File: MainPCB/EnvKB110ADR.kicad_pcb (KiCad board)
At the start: 2 copper layers, 429.5 x 123.7 mm, 231 parts, among them U1 XC6206PxxxMR, U2 STM32F411CEUx

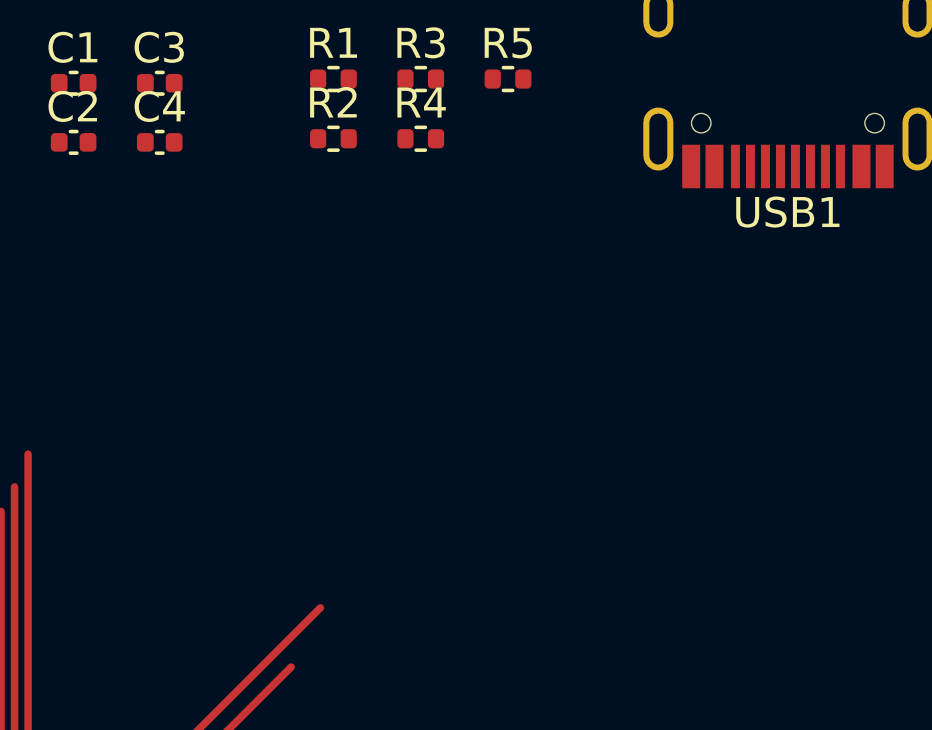
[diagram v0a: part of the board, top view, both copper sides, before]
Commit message: Updated PCB to have new parts
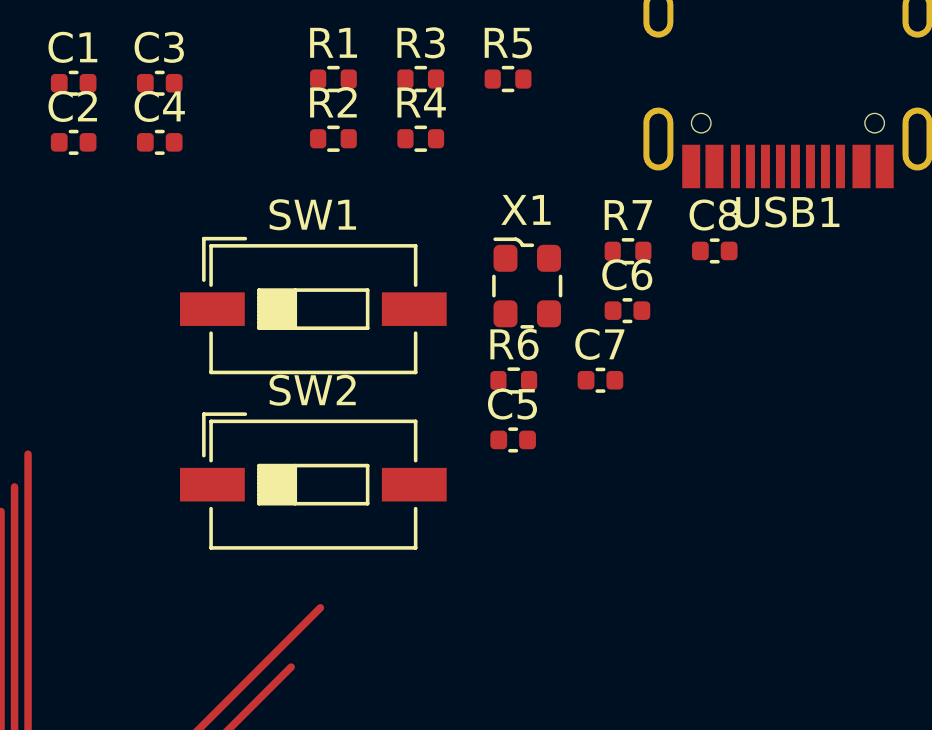
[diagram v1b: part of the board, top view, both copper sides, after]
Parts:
- added C5: 1uf capacitor, Capacitor_SMD:C_0402_1005Metric, F.Cu at (426.3, 69.7)
- added C6: 1uf capacitor, Capacitor_SMD:C_0402_1005Metric, F.Cu at (430.1, 65.4)
- added C7: 100nf 0402, Capacitor_SMD:C_0402_1005Metric, F.Cu at (429.2, 67.7)
- added C8: 100nf 0402, Capacitor_SMD:C_0402_1005Metric, F.Cu at (433.0, 63.4)
- added R6: 100k 0402, Resistor_SMD:R_0402_1005Metric, F.Cu at (426.3, 67.7)
- added R7: 10K 0402, Resistor_SMD:R_0402_1005Metric, F.Cu at (430.1, 63.4)
- added SW1: Boot Mode, Button_Switch_SMD:SW_DIP_SPSTx01_Slide_6.7x4.1mm_W6.73mm_P2.54mm_LowProfile_JPin, F.Cu at (419.6, 65.3)
- added SW2: Reset Switch, Button_Switch_SMD:SW_DIP_SPSTx01_Slide_6.7x4.1mm_W6.73mm_P2.54mm_LowProfile_JPin, F.Cu at (419.6, 71.2)
- added X1: ECS-2520MV-xxx-xx, Oscillator:Oscillator_SMD_ECS_2520MV-xxx-xx-4Pin_2.5x2.0mm, F.Cu at (426.8, 64.5)
- R1: value 1.5K -> 1.5K 0402
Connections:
- C1 pad 1: GND -> +3V3
- C1 pad 2: +3V3 -> GND
- U2 pad 44: (no net) -> boot0
- U2 pad 5: (no net) -> OSCpin
- U2 pad 7: (no net) -> resetsw

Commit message: Added row/col pins in the schematic for pcbnew to show them
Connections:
- U2 pad 10: (no net) -> col15
- U2 pad 11: (no net) -> col16
- U2 pad 12: (no net) -> col17
- U2 pad 14: (no net) -> col19
- U2 pad 15: (no net) -> col20
- U2 pad 16: (no net) -> col21
- U2 pad 17: (no net) -> col22
- U2 pad 18: (no net) -> col0
- U2 pad 19: (no net) -> col1
- U2 pad 20: (no net) -> col2
- U2 pad 21: (no net) -> col10
- U2 pad 23: GND -> (no net)
- U2 pad 25: (no net) -> col11
- U2 pad 26: (no net) -> col12
- U2 pad 27: (no net) -> col13
- U2 pad 28: (no net) -> col14
- U2 pad 29: (no net) -> row6
- U2 pad 30: (no net) -> row1
- U2 pad 31: (no net) -> row7
- U2 pad 34: (no net) -> row3
- U2 pad 35: GND -> (no net)
- U2 pad 37: (no net) -> row4
- U2 pad 38: (no net) -> row5
- U2 pad 39: (no net) -> col3
- U2 pad 40: (no net) -> col4
- U2 pad 41: (no net) -> col5
- U2 pad 42: (no net) -> col6
- U2 pad 43: (no net) -> col7
- U2 pad 45: (no net) -> col8
- U2 pad 46: (no net) -> col9
- U2 pad 47: GND -> (no net)

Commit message: See List
- Added ANSI support
- redone sections of the board to fit ansi support
- edited all footprints to have through holes so they can be connected on both sides.
- probably a bunch of other shite
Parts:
- added D_ANSI_1: SOD-123, Diode_SMD:D_SOD-123, B.Cu at (318.5, 114.1)
- added K_ANSI_1: KEYSW, MX_Only:MXOnly-2.25U-Hotswap, F.Cu at (59.0, 146.8)
- added K_ANSI_2: KEYSW, MX_Only:MXOnly-2.25U-Hotswap, F.Cu at (301.9, 127.7)
- added K_ANSI_3: KEYSW, MX_Only:MXOnly-1.5U-Hotswap, F.Cu at (309.1, 108.7)
- moved D_62 27.0 mm to (299.7, 135.8)
- moved D_82 11.1 mm to (296.1, 118.0), turned to 180 degrees
- moved D_86 7.37 mm to (58.4, 155.4), turned to 180 degrees
- turned K_62 to 90 degrees
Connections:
- D_62 pad 1: row4 -> row5
- H1 pad 1: (no net) -> GND
- H10 pad 1: (no net) -> GND
- H2 pad 1: (no net) -> GND
- H3 pad 1: (no net) -> GND
- H4 pad 1: (no net) -> GND
- H5 pad 1: (no net) -> GND
- H6 pad 1: (no net) -> GND
- H8 pad 1: (no net) -> GND
- H9 pad 1: (no net) -> GND
- U2 pad 1: (no net) -> Net-(U2-Pad1)
- U2 pad 13: (no net) -> col18
- U2 pad 2: (no net) -> Net-(U2-Pad2)
- U2 pad 22: (no net) -> Net-(U2-Pad22)
- U2 pad 23: (no net) -> Net-(U2-Pad23)
- U2 pad 3: (no net) -> Net-(U2-Pad3)
- U2 pad 35: (no net) -> Net-(U2-Pad35)
- U2 pad 4: (no net) -> Net-(U2-Pad4)
- U2 pad 47: (no net) -> Net-(U2-Pad47)
- U2 pad 6: (no net) -> Net-(U2-Pad6)
- USB1 pad 3: (no net) -> Net-(USB1-Pad3)
- USB1 pad 9: (no net) -> Net-(USB1-Pad9)
- X1 pad 1: (no net) -> Net-(X1-Pad1)
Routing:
- net col0: track 145.5 -> 173.5 mm, vias 6 -> 0
- net col14: track 133.8 -> 106.4 mm, vias 3 -> 0
- net Net-(D_62-Pad2): track 11.5 -> 29.6 mm, vias 0 -> 1
- net row5: track 438.4 -> 455.3 mm
- net col1: track 123.4 -> 138.8 mm, vias 3 -> 0
- net Net-(D_ANSI_1-Pad2): track 0.00 -> 11.3 mm
- net Net-(D_86-Pad2): track 7.11 -> 17.7 mm
- net col13: track 116.6 -> 108.0 mm, vias 4 -> 0
- net col12: track 71.3 -> 63.2 mm, vias 3 -> 0
- net col11: track 113.8 -> 106.1 mm, vias 5 -> 0
- net col15: track 112.1 -> 104.8 mm, vias 4 -> 0
- net col10: track 113.5 -> 106.3 mm, vias 5 -> 0
- net row6: track 473.9 -> 476.6 mm
- net row4: track 434.8 -> 437.1 mm, vias 1 -> 2
- net row1: vias 1 -> 0
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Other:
- board size 429.5 x 123.7 mm -> 429.5 x 125 mm

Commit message: more progress, working on column traces.
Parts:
- SW1, SW2: footprint Button_Switch_SMD:SW_DIP_SPSTx01_Slide_6.7x4.1mm_W6.73mm_P2.54mm_LowProfile_JPin -> Button_Switch_SMD:SW_Push_SPST_NO_Alps_SKRK
- moved D_12 9.52 mm to (55.6, 63.1)
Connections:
- U2 pad 23: Net-(U2-Pad23) -> GND
- U2 pad 35: Net-(U2-Pad35) -> GND
- U2 pad 47: Net-(U2-Pad47) -> GND
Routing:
- net col2: track 86.2 -> 422.8 mm
- net col0: track 173.5 -> 503.4 mm
- net col3: track 111.2 -> 428.7 mm
- net col1: track 138.8 -> 441.0 mm
- net col4: track 86.1 -> 384.3 mm
- net col5: track 86.1 -> 365.1 mm
- net col7: track 85.9 -> 330.6 mm
- net col6: track 106.1 -> 337.3 mm
- net col8: track 86.3 -> 311.3 mm
- net col9: track 86.3 -> 292.1 mm
- net col10: track 106.3 -> 292.9 mm
- net col11: track 106.1 -> 269.7 mm
- net col12: track 63.2 -> 208.8 mm
- net col13: track 108.0 -> 231.1 mm, vias 0 -> 1
- net col14: track 106.4 -> 226.6 mm
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
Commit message: finished up traces and added a cat silkscreen.
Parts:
- added G***: LOGO, logo:logo, F.Cu at (445.4, 63.2)
- moved U1 43.2 mm to (399.9, 61.1)
- moved USB1 43.0 mm to (392.4, 51.5)
- moved R5 36.5 mm to (389.8, 60.7)
- moved U2 35.5 mm to (417.5, 65.1)
- moved C5 30.6 mm to (396.8, 61.6), turned to 90 degrees
- moved C6 28.1 mm to (402.4, 60.7), turned to 90 degrees
- moved R2 26.7 mm to (393.7, 61.3), turned to 90 degrees
- moved C8 25.1 mm to (409.1, 55.6), turned to 180 degrees
- moved SW2 21.6 mm to (407.4, 53.4)
- moved R7 21.1 mm to (410.1, 56.7)
- moved C7 18.7 mm to (417.4, 53.3), turned to 90 degrees
- moved R3 18.6 mm to (406.1, 64.8), turned to 180 degrees
- moved R4 17.6 mm to (406.1, 63.8), turned to 180 degrees
- moved R6 17.5 mm to (416.4, 53.3), turned to 90 degrees
- moved X1 17.3 mm to (409.7, 61.9), turned to 270 degrees
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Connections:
- U2 pad 10: col15 -> row1
- U2 pad 11: col16 -> row3
- U2 pad 12: col17 -> row4
- U2 pad 13: col18 -> row5
- U2 pad 14: col19 -> row6
- U2 pad 15: col20 -> row7
- U2 pad 16: col21 -> col13
- U2 pad 17: col22 -> col0
- U2 pad 18: col0 -> col1
- U2 pad 19: col1 -> col2
- U2 pad 20: col2 -> col3
- U2 pad 21: col10 -> col4
- U2 pad 25: col11 -> col5
- U2 pad 26: col12 -> col6
- U2 pad 27: col13 -> col7
- U2 pad 28: col14 -> col8
- U2 pad 29: row6 -> col9
- U2 pad 30: row1 -> col10
- U2 pad 31: row7 -> col11
- U2 pad 34: row3 -> col12
- U2 pad 37: row4 -> col14
- U2 pad 38: row5 -> col15
- U2 pad 39: col3 -> col16
- U2 pad 40: col4 -> col17
- U2 pad 41: col5 -> col18
- U2 pad 42: col6 -> col19
- U2 pad 43: col7 -> col20
- U2 pad 45: col8 -> col21
- U2 pad 46: col9 -> col22
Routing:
- net col19: track 206.0 -> 148.8 mm, vias 0 -> 1
- net col17: track 139.5 -> 194.2 mm, vias 0 -> 1
- net col16: track 158.1 -> 211.2 mm, vias 0 -> 1
- net col15: track 177.6 -> 227.6 mm, vias 0 -> 1
- net col22: track 120.8 -> 167.7 mm, vias 0 -> 1
- net col14: track 226.6 -> 273.1 mm, vias 0 -> 1
- net +3V3: track 0.00 -> 42.8 mm, vias 0 -> 5
- net col12: track 208.8 -> 251.1 mm, vias 0 -> 1
- net col11: track 269.7 -> 311.1 mm, vias 0 -> 1
- net col10: track 292.9 -> 332.4 mm, vias 0 -> 1
- net col20: track 70.1 -> 109.2 mm, vias 0 -> 1
- net col21: track 83.4 -> 121.6 mm, vias 0 -> 1
- net col9: track 292.1 -> 329.7 mm, vias 0 -> 1
- net col8: track 311.3 -> 347.1 mm, vias 0 -> 1
- net col7: track 330.6 -> 364.5 mm, vias 0 -> 1
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- added copper zone on B.Cu, net +3V3
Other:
- net class Default: trace_width 0.25 -> 0.127
- rule trace_min: 0.2 -> 0.127
- rule via_min_drill: 0.3 -> 0.2

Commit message: Corrected a trace going through a hole
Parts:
- moved H8 1.74 mm to (428.1, 118.2)
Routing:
- net col21: track 121.6 -> 123.1 mm
- net row5: track 465.1 -> 466.6 mm
